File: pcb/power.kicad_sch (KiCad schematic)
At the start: 22 parts, among them U1 LDLN025M25R, U13 TS3312AQPR, U2 LM27762DSST

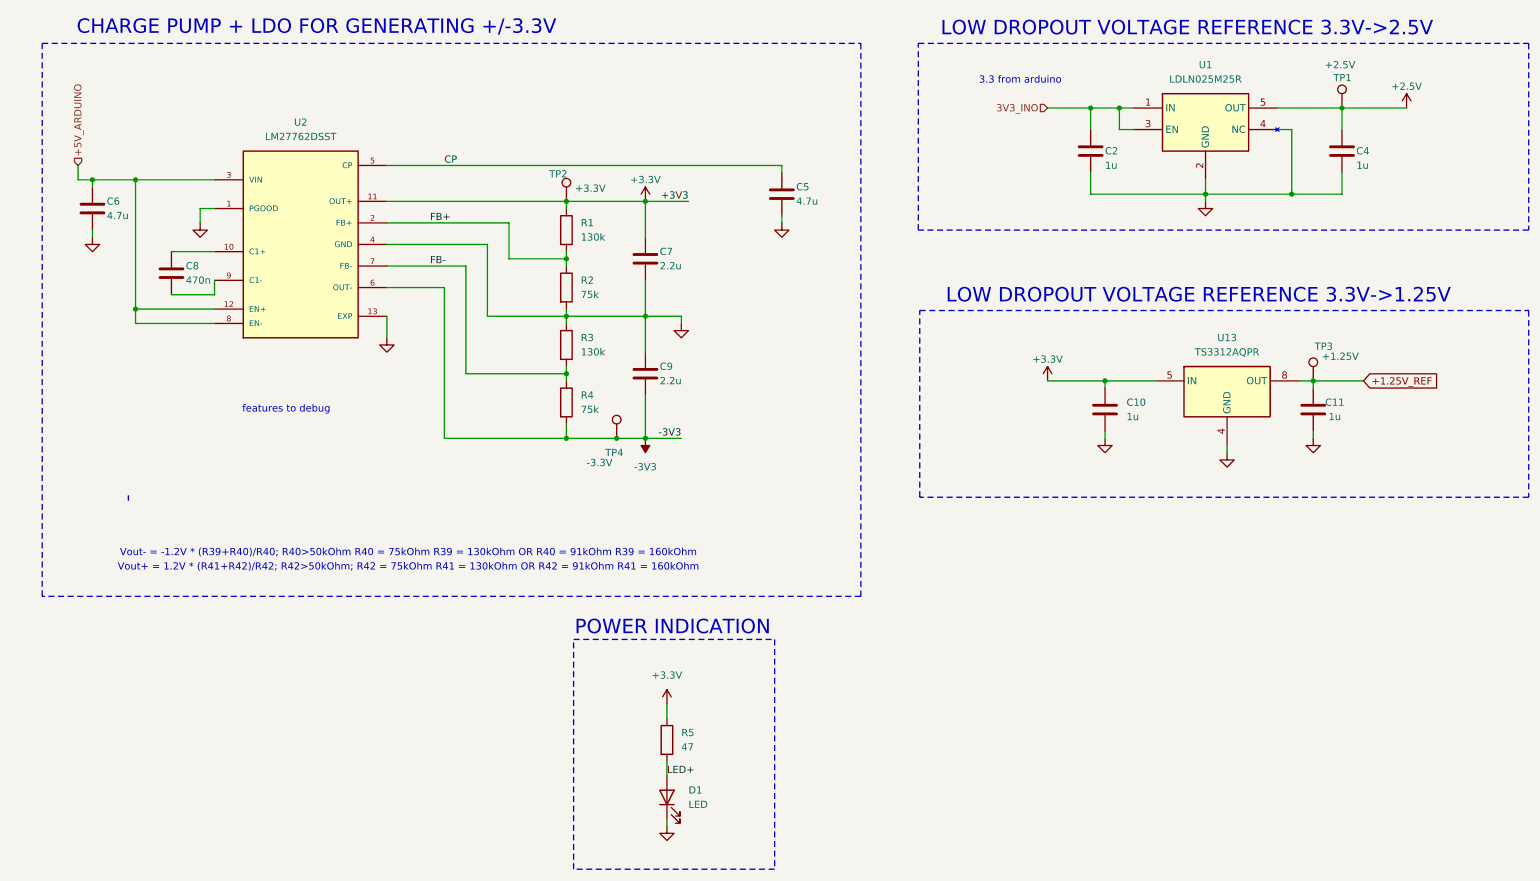
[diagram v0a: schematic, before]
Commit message: feat: Prepare 0.9 PCB with fixed issues from 0.8 tests (#102)
* feat: Upgrade speaker simulation to realistic one

* feat: Improve PCB design after tests of rev 0.8

- Added new generation of humidity sensor
- New silkscreen information for different components
- Added additional testpoints
- Removed PWM path for ultrasound transmitter

* refactor: cleanup of symbol and footprint library

- removed components that are not used anymore
- ran final DRC to prepare for manufacturing

* feat: Update BOM with extra res, caps, tps and sht

* fix: Rename schematics to match the docs
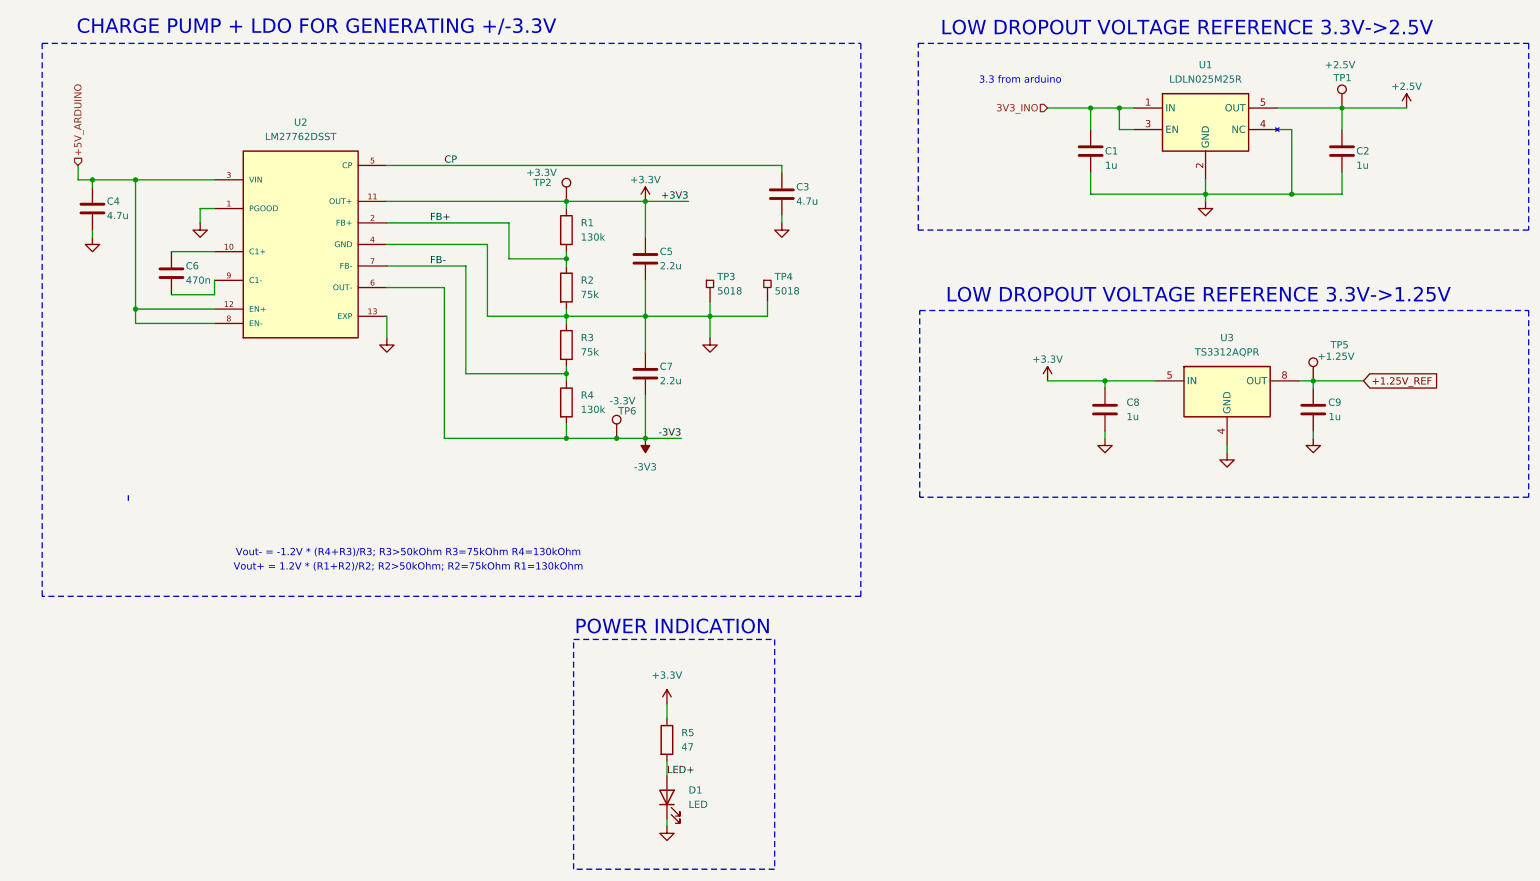
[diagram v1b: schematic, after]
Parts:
- added TP3, TP4: 5018, SensEdu:5018, symbol SensEdu:5018
- C1: renamed from C2; footprint Capacitor_SMD:C_0603_1608Metric -> SensEdu:C_0603_1608Metric
- C2: renamed from C4; footprint Capacitor_SMD:C_0603_1608Metric -> SensEdu:C_0603_1608Metric
- C3: renamed from C5; footprint Capacitor_SMD:C_0805_2012Metric -> SensEdu:C_0805_2012Metric
- C4: renamed from C6; footprint Capacitor_SMD:C_0805_2012Metric -> SensEdu:C_0805_2012Metric
- C5: renamed from C7; footprint Capacitor_SMD:C_0805_2012Metric -> SensEdu:C_0805_2012Metric
- C6: renamed from C8; footprint Capacitor_SMD:C_0603_1608Metric -> SensEdu:C_0603_1608Metric
- C7: renamed from C9; footprint Capacitor_SMD:C_0805_2012Metric -> SensEdu:C_0805_2012Metric
- C8: renamed from C10; footprint Capacitor_SMD:C_0603_1608Metric -> SensEdu:C_0603_1608Metric
- C9: renamed from C11; footprint Capacitor_SMD:C_0603_1608Metric -> SensEdu:C_0603_1608Metric
- D1: footprint LED_SMD:LED_0805_2012Metric -> SensEdu:LED_0805_2012Metric
- R1, R2, R5: footprint Resistor_SMD:R_0603_1608Metric -> SensEdu:R_0603_1608Metric
- R3: value 130k -> 75k; footprint Resistor_SMD:R_0603_1608Metric -> SensEdu:R_0603_1608Metric
- R4: value 75k -> 130k; footprint Resistor_SMD:R_0603_1608Metric -> SensEdu:R_0603_1608Metric
- TP1, TP2: footprint TestPoint:TestPoint_THTPad_D2.0mm_Drill1.0mm -> SensEdu:TestPoint_THTPad_D2.0mm_Drill1.0mm
- TP5: renamed from TP3; footprint TestPoint:TestPoint_THTPad_D2.0mm_Drill1.0mm -> SensEdu:TestPoint_THTPad_D2.0mm_Drill1.0mm
- TP6: renamed from TP4; footprint TestPoint:TestPoint_THTPad_D2.0mm_Drill1.0mm -> SensEdu:TestPoint_THTPad_D2.0mm_Drill1.0mm
- U1: footprint SamacSys_Parts:SOT95P280X145-5N -> SensEdu:SOT95P280X145-5N
- U3: renamed from U13; footprint SamacSys_Parts:TS3312AQPR -> SensEdu:TS3312AQPR
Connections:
- net GND: now also TP3.1, TP4.1
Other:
- note added: "Vout+ = 1.2V * (R1+R2)/R2; R2>50kOhm; R2=75kOhm R1=130kOhm"
- note added: "Vout- = -1.2V * (R4+R3)/R3; R3>50kOhm R3=75kOhm R4=130kOhm"
- note removed: "Vout+ = 1.2V * (R41+R42)/R42; R42>50kOhm; R42 = 75kOhm R41 = 130kOhm OR R42 = 91kOhm R41 = 160kOhm"
- note removed: "Vout- = -1.2V * (R39+R40)/R40; R40>50kOhm R40 = 75kOhm R39 = 130kOhm OR R40 = 91kOhm R39 = 160kOhm"
- note removed: "features to debug"
